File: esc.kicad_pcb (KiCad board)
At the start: 2 copper layers, 50 x 60.5 mm, 78 parts, among them IC1 4N25, IC2 LM25101, IC3 LM25101, IC4 LM25101, IC5 ATMEGA8-AI, P1 CONN_01X03, P2 CONN_01X03, P3 CONN_01X02, P4 CONN_02X02, P5 CONN_01X01, P6 CONN_01X01, Q1 MOSFET_N, Q10 MOSFET_N, Q11 MOSFET_N, Q12 MOSFET_N, Q2 MOSFET_N, Q3 MOSFET_N, Q4 MOSFET_N, Q5 MOSFET_N, Q6 MOSFET_N, Q7 MOSFET_N, Q8 MOSFET_N, Q9 MOSFET_N, U1 MCP1804, U2 LM2940 10V, Y1 RESONATEUR

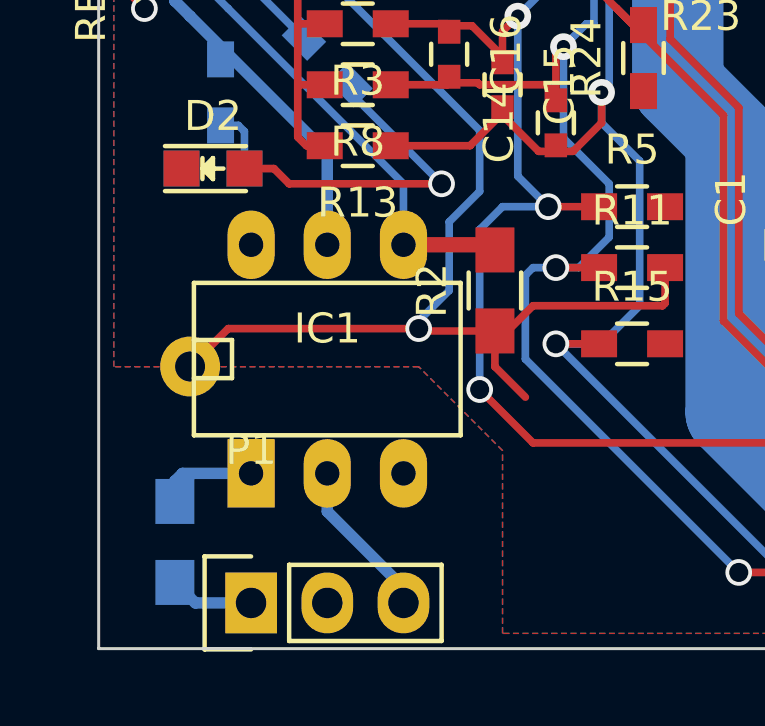
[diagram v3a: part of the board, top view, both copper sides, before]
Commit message: Optokoppler zu LTV-356T weil muss so
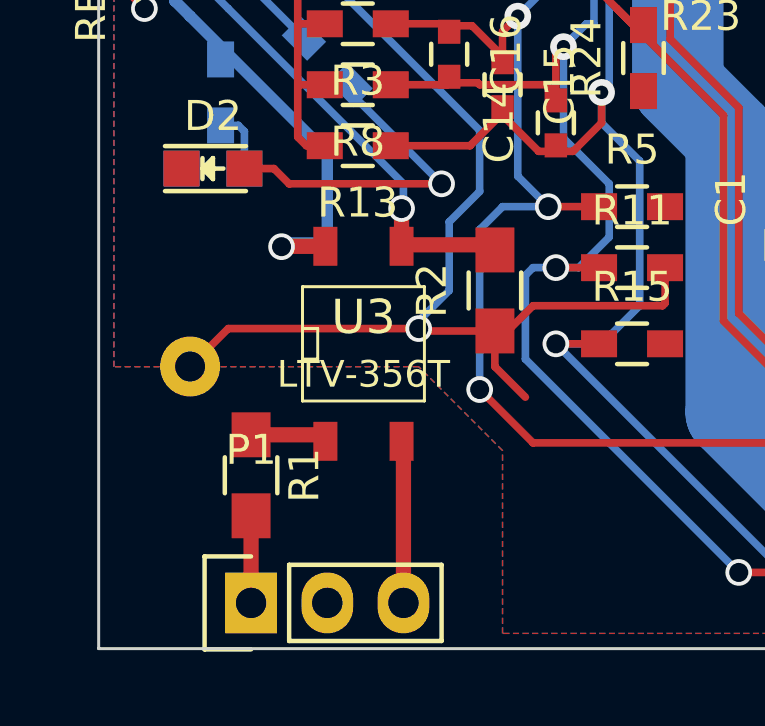
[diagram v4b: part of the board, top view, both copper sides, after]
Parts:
- removed IC1: 4N25, Sockets_DIP:DIP-6__300_ELL
- added U3: LTV-356T, toni:SO-4, F.Cu at (195.0, 100.3)
- R1: moved to F.Cu
- moved R1 3.38 mm to (191.3, 104.7)
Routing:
- net +5V: track 65.1 -> 68.1 mm, vias 5 -> 6
- net Net-(R1-Pad1): track 3.33 -> 2.57 mm
- net /INPUT_GND: track 5.37 -> 5.92 mm
- net PWM: track 32.9 -> 33.0 mm, vias 1 -> 2

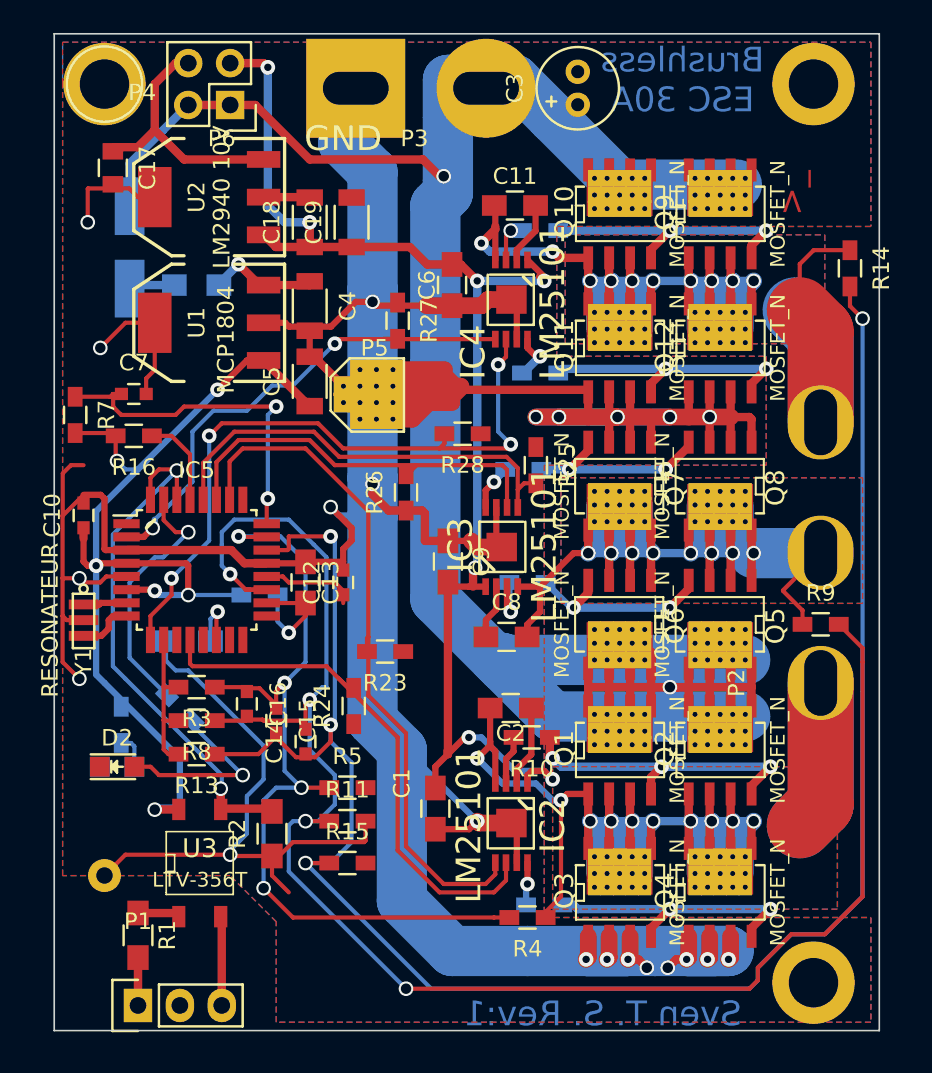
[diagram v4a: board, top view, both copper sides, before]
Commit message: Getrennte Masse für Digital-Teil
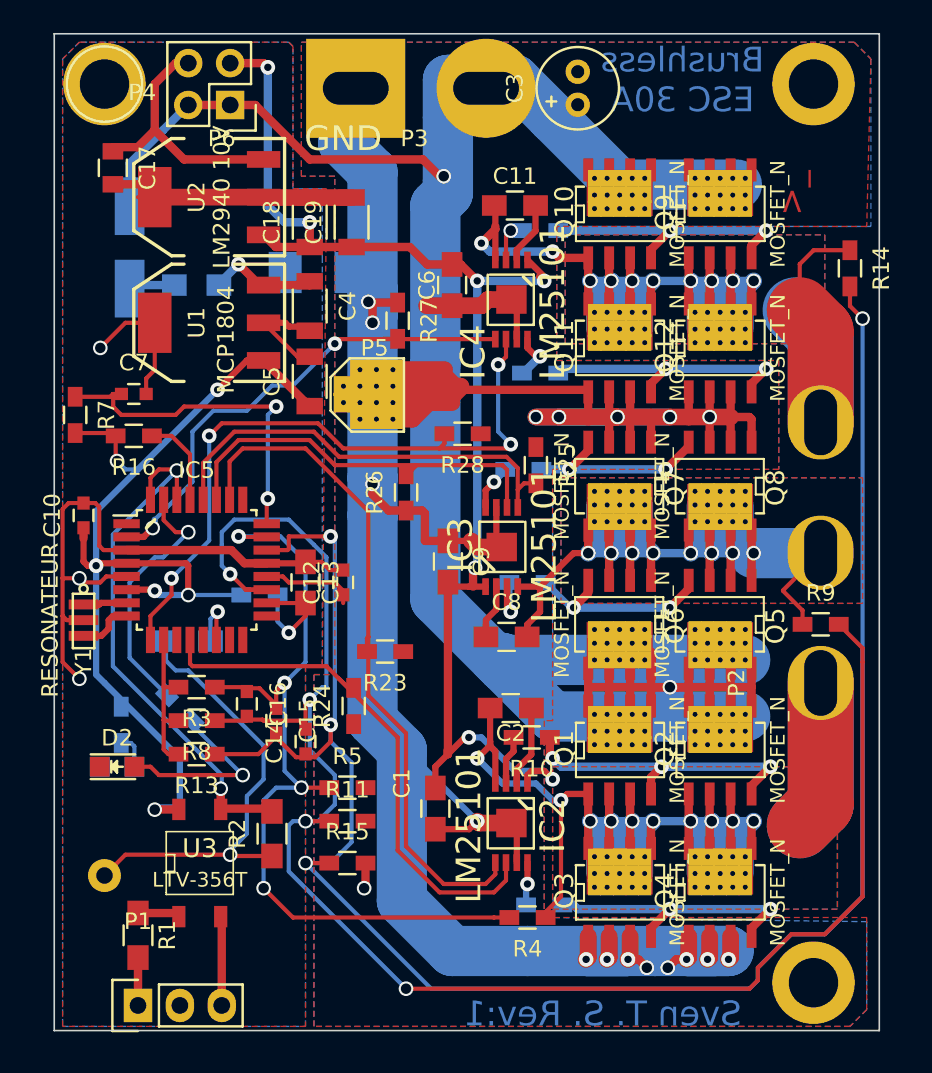
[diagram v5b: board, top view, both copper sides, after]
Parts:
- added R31: Bridge, Resistors_SMD:R_1210_HandSoldering, B.Cu at (202.2, 64.5)
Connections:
- C10 pad 2: GND -> D_GND
- C12 pad 2: GND -> D_GND
- C13 pad 1: GND -> D_GND
- C4 pad 2: GND -> D_GND
- C5 pad 2: GND -> D_GND
- C7 pad 2: GND -> D_GND
- D2 pad 1: GND -> D_GND
- D3 pad 1: GND -> D_GND
- IC5 pad 21: GND -> D_GND
- IC5 pad 3: GND -> D_GND
- IC5 pad 5: GND -> D_GND
- P6 pad 1: GND -> D_GND
- R17 pad 2: GND -> D_GND
- R2 pad 1: GND -> D_GND
- U1 pad 2: GND -> D_GND
- Y1 pad 2: GND -> D_GND
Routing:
- net GND: track 360.8 -> 267.8 mm, vias 22 -> 18
- net D_GND: track 0.00 -> 85.2 mm, vias 0 -> 4
- added copper zone on B.Cu, net D_GND
- added copper zone on F.Cu, net D_GND
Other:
- board text added: "Analog Side"
- board text added: "Digital Side"

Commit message: Spannungswandler U1 geändert auf LD1117
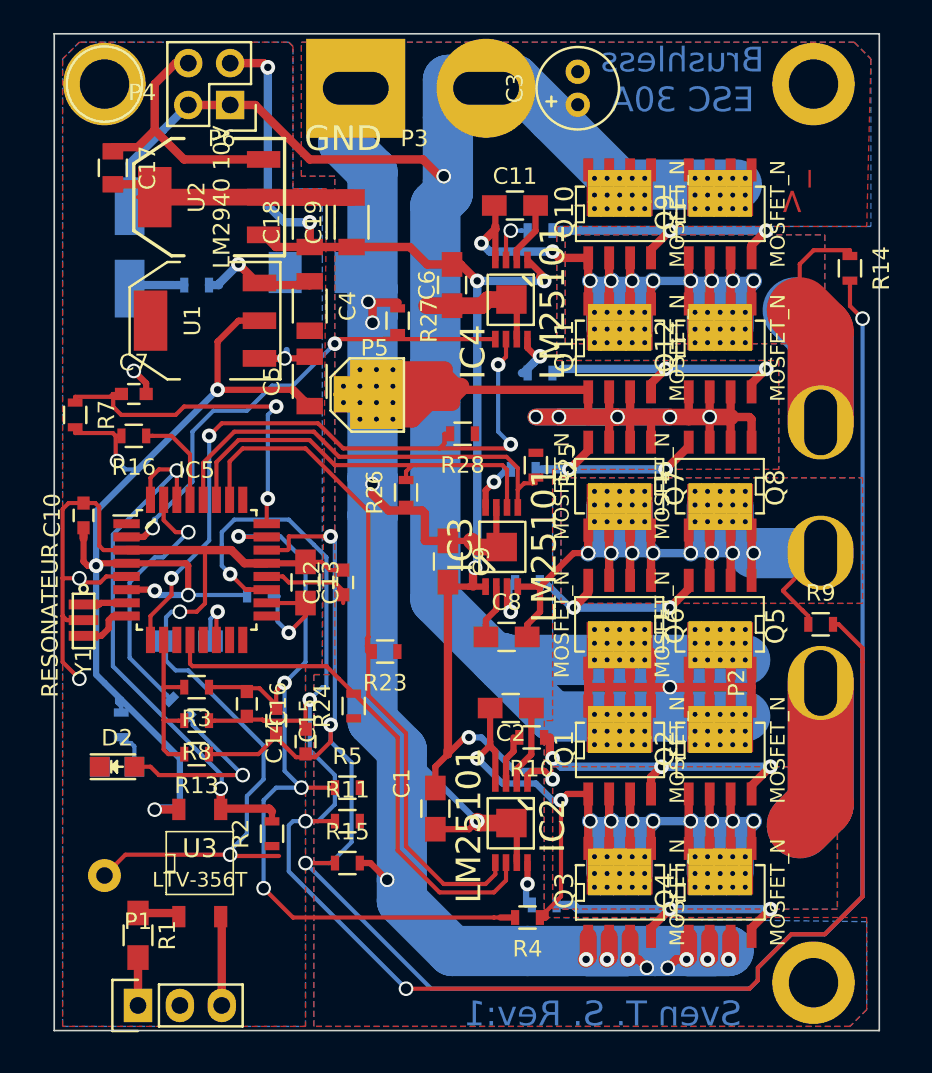
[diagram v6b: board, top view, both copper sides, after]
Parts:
- Q1, Q10, Q11, Q12, Q2, Q3, Q4, Q5, Q6, Q7, Q8, Q9: footprint sven:SO8_WITH_Heatpipes_New -> Sven:SO8_WITH_Heatpipes_New
- R10, R11, R12, R13, R14, R15, R16, R18, R19, R20, R21, R22, R23, R24, R25, R26, R27, R28, R29, R3, R30, R4, R5, R7, R8, R9: footprint Resistors_SMD:R_0603_HandSoldering -> Resistors_SMD:R_0603
- R2, R6: footprint Resistors_SMD:R_0805_HandSoldering -> Resistors_SMD:R_0603
- U1: value MCP1804 -> LD1117S50TR; footprint toni:SOT223_GND_VO_VI -> TO_SOT_Packages_SMD:SOT-223
- moved U1 0.28 mm to (195.3, 67.4)
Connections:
- U1 pad 1: +5V -> D_GND
- U1 pad 2: D_GND -> +5V
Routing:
- net +5V: track 68.1 -> 74.9 mm
- net GND: track 267.8 -> 271.0 mm
- net S_A: track 52.1 -> 53.7 mm
- net M: track 9.48 -> 10.7 mm
- net S_C: track 115.2 -> 116.3 mm
- net S_B: track 103.2 -> 104.2 mm
- net Net-(C4-Pad1): track 6.62 -> 7.63 mm
- net PWM: track 33.0 -> 33.8 mm
- net Net-(IC4-Pad8): track 3.03 -> 3.81 mm
- net A-: track 32.9 -> 32.1 mm
- net A: track 120.8 -> 121.5 mm
- net /B_Lowside_Gate: track 11.9 -> 12.5 mm
- net Net-(D1-Pad2): track 2.84 -> 3.44 mm
- net Net-(IC3-Pad3): track 3.43 -> 4.03 mm
- net Net-(C13-Pad2): track 7.14 -> 7.68 mm
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
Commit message: Kondensator C3 geändert (Auf richtigen Footprint) + Bestückungsdruck
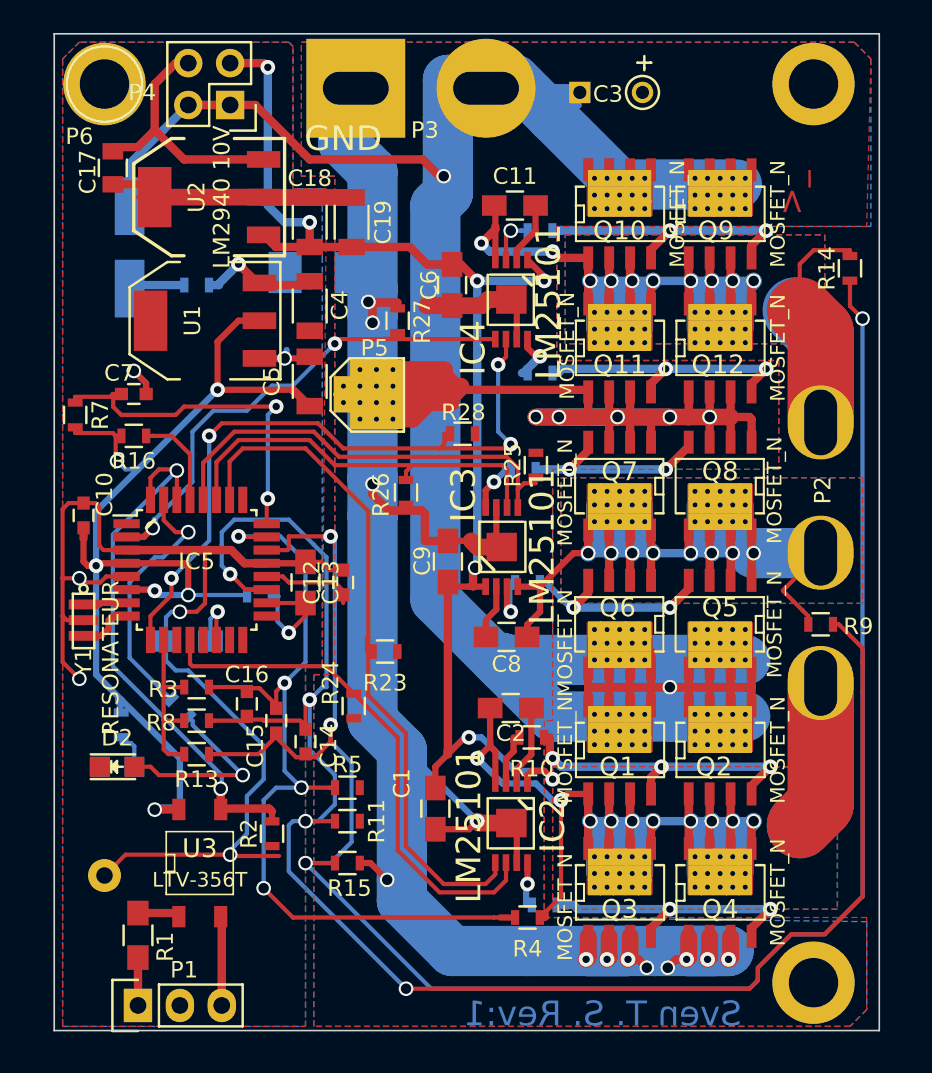
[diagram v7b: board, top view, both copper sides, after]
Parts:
- C3: footprint Capacitors_Elko_ThroughHole:Elko_vert_11x5mm_RM2_CopperClear -> Capacitors_ThroughHole:C_Radial_D8_L13_P3.8
- moved C3 0.77 mm to (218.1, 53.6), turned to 0 degrees
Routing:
- net V_BAT: track 161.0 -> 167.1 mm
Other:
- rule pad_to_mask_clearance: 0 -> 0.1
- board text added: "Philipp Hörauf"
- board text added: "Toni Bartsch"
- board text removed: "Brushless ESC 30A"

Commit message: Gerber erzeugt
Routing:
- net C: track 101.4 -> 105.4 mm
- net GND: track 271.0 -> 274.8 mm
- net V_BAT: track 167.1 -> 170.8 mm
- net A: track 121.5 -> 125.2 mm
- net B: track 84.5 -> 87.6 mm
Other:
- board text added: "(C) Sven Schneider"
- board text added: "Toni Bratsch"
